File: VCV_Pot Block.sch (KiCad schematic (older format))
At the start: 18 parts, among them J14 Conn_01x08_Female, U3 CD74HC4067M

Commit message: Sub boards completed
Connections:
- net at U3.13 (S3): now also J14.3 (Pin_3); no longer J14.4 (Pin_4)
- net at U3.14 (S2): now also J14.4 (Pin_4); no longer J14.3 (Pin_3)
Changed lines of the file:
@@
 	1300 2400 2050 2400
 Wire Wire Line
-	1300 2600 2050 2600
-Wire Wire Line
 	1300 2500 2050 2500
-Wire Wire Line
-	1300 2700 2050 2700
 Wire Wire Line
 	1950 2800 1300 2800
@@
 Connection ~ 2550 1500
 NoConn ~ 1300 3100
+Wire Wire Line
+	1300 2600 1650 2600
+Wire Wire Line
+	1650 2600 1650 2700
+Wire Wire Line
+	1650 2700 2050 2700
+Wire Wire Line
+	2050 2600 1750 2600
+Wire Wire Line
+	1750 2600 1750 2650
+Wire Wire Line
+	1750 2650 1300 2650
+Wire Wire Line
+	1300 2650 1300 2700
 $EndSCHEMATC

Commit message: Tidy schematic / renumber components / complete daughter boards
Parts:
- J5: renamed from J14; value Conn_01x08_Female -> ~; symbol Connector:Conn_01x08_Female -> Connector:Conn_01x08_Male
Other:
- moved on the sheet: PT_1, PT_10, PT_11, PT_12, PT_13, PT_14, PT_15, PT_16, PT_2, PT_3, PT_4, PT_5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

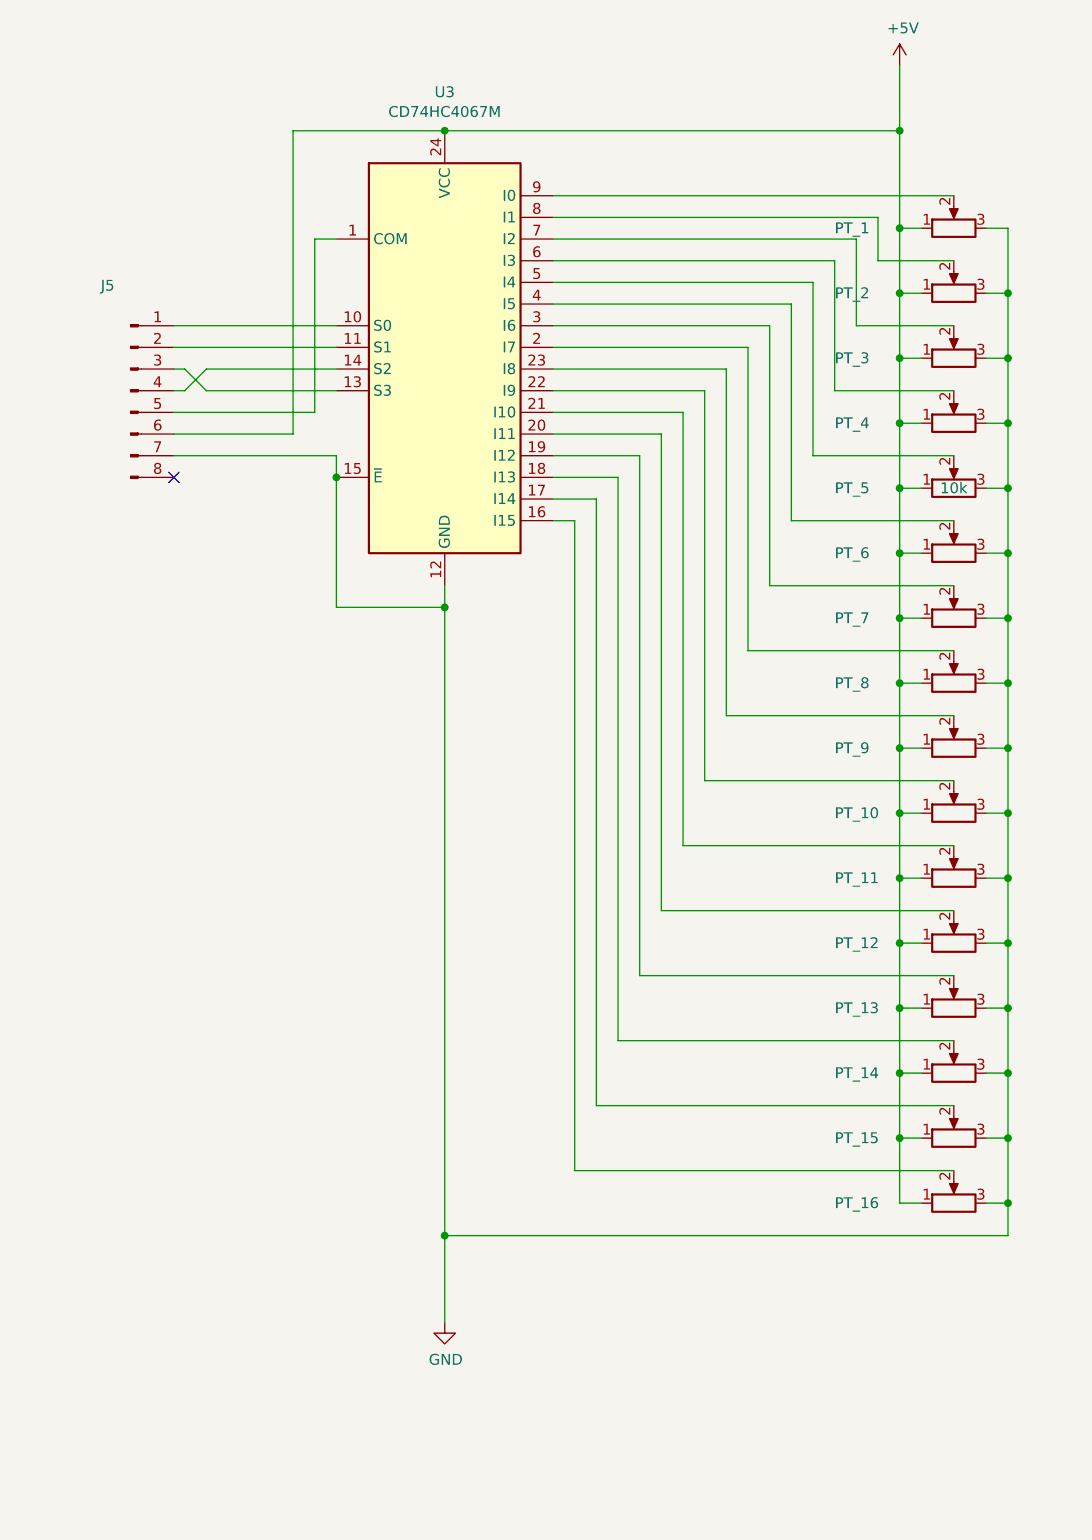
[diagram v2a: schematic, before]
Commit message: Redesign of upper boards
Added bussed resistors following Igor's correction to the schematic + tidied schematic.
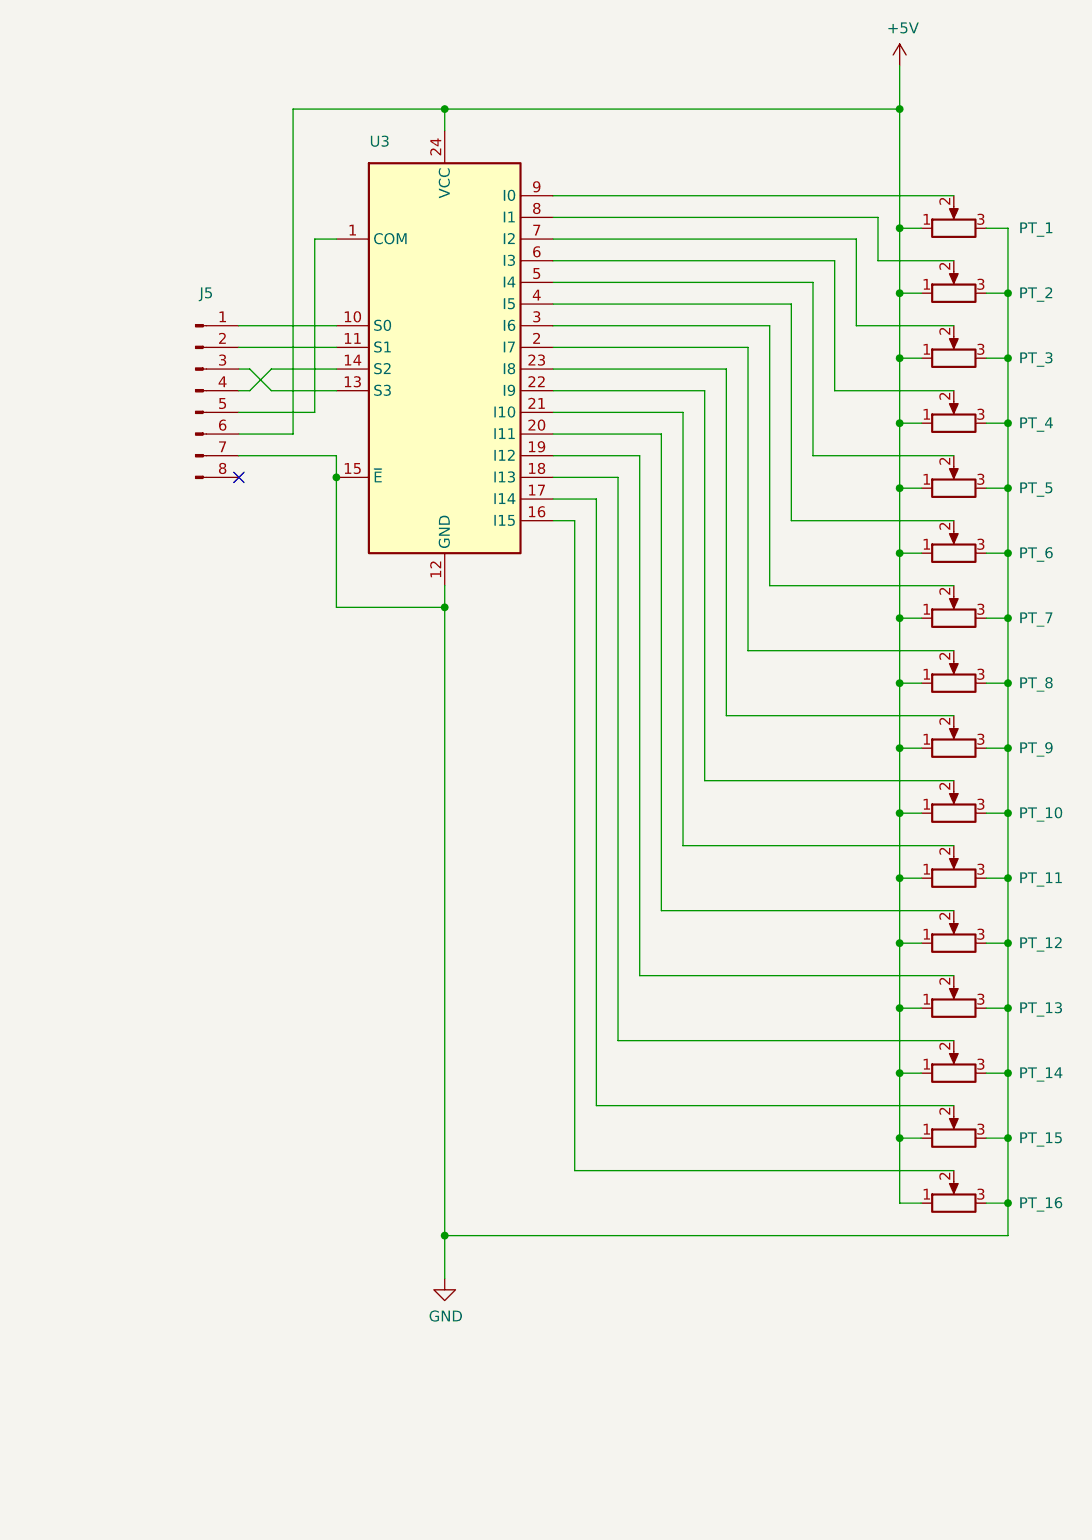
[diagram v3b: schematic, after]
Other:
- moved on the sheet: J5
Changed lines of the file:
@@
 U 1 1 5C26C20B
 P 5050 1700
-F 0 "PT_1" V 5050 2250 50  0000 R CNN
+F 0 "PT_1" V 5050 1400 50  0000 R CNN
 F 1 "10k" H 4980 1655 50  0001 R CNN
 F 2 "cunabulapress-footprints:Potentiometer_Alps_RK09K_Single_Vertical_Edit" H 5050 1700 50  0001 C CNN
@@
 U 1 1 5C26C26F
 P 5050 2000
-F 0 "PT_2" V 5050 2550 50  0000 R CNN
+F 0 "PT_2" V 5050 1700 50  0000 R CNN
 F 1 "10k" H 4980 1955 50  0001 R CNN
 F 2 "cunabulapress-footprints:Potentiometer_Alps_RK09K_Single_Vertical_Edit" H 5050 2000 50  0001 C CNN
@@
 U 1 1 5C26C8F7
 P 5050 2300
-F 0 "PT_3" V 5050 2850 50  0000 R CNN
+F 0 "PT_3" V 5050 2000 50  0000 R CNN
 F 1 "10k" H 4980 2255 50  0001 R CNN
 F 2 "cunabulapress-footprints:Potentiometer_Alps_RK09K_Single_Vertical_Edit" H 5050 2300 50  0001 C CNN
@@
 U 1 1 5C26CB54
 P 5050 2600
-F 0 "PT_4" V 5050 3150 50  0000 R CNN
+F 0 "PT_4" V 5050 2300 50  0000 R CNN
 F 1 "10k" H 4980 2555 50  0001 R CNN
 F 2 "cunabulapress-footprints:Potentiometer_Alps_RK09K_Single_Vertical_Edit" H 5050 2600 50  0001 C CNN
@@
 U 1 1 5C26CB7C
 P 5050 2900
-F 0 "PT_5" V 5050 3450 50  0000 R CNN
-F 1 "10k" V 5050 2900 50  0000 C CNN
+F 0 "PT_5" V 5050 2600 50  0000 R CNN
+F 1 "10k" V 5050 2900 50  0001 C CNN
 F 2 "cunabulapress-footprints:Potentiometer_Alps_RK09K_Single_Vertical_Edit" H 5050 2900 50  0001 C CNN
 F 3 "~" H 5050 2900 50  0001 C CNN
@@
 U 1 1 5C26CBA6
 P 5050 3200
-F 0 "PT_6" V 5050 3750 50  0000 R CNN
+F 0 "PT_6" V 5050 2900 50  0000 R CNN
 F 1 "10k" H 4980 3155 50  0001 R CNN
 F 2 "cunabulapress-footprints:Potentiometer_Alps_RK09K_Single_Vertical_Edit" H 5050 3200 50  0001 C CNN
@@
 U 1 1 5C26CBD2
 P 5050 3500
-F 0 "PT_7" V 5050 4050 50  0000 R CNN
+F 0 "PT_7" V 5050 3200 50  0000 R CNN
 F 1 "10k" H 4980 3455 50  0001 R CNN
 F 2 "cunabulapress-footprints:Potentiometer_Alps_RK09K_Single_Vertical_Edit" H 5050 3500 50  0001 C CNN
@@
 U 1 1 5C26CDC5
 P 5050 3800
-F 0 "PT_8" V 5050 4350 50  0000 R CNN
+F 0 "PT_8" V 5050 3500 50  0000 R CNN
 F 1 "10k" H 4980 3755 50  0001 R CNN
 F 2 "cunabulapress-footprints:Potentiometer_Alps_RK09K_Single_Vertical_Edit" H 5050 3800 50  0001 C CNN
@@
 U 1 1 5C26D143
 P 5050 4100
-F 0 "PT_9" V 5050 4650 50  0000 R CNN
+F 0 "PT_9" V 5050 3800 50  0000 R CNN
 F 1 "10k" H 4980 4055 50  0001 R CNN
 F 2 "cunabulapress-footprints:Potentiometer_Alps_RK09K_Single_Vertical_Edit" H 5050 4100 50  0001 C CNN
@@
 U 1 1 5C26D193
 P 5050 4400
-F 0 "PT_10" V 5050 4950 50  0000 R CNN
+F 0 "PT_10" V 5050 4100 50  0000 R CNN
 F 1 "10k" H 4980 4355 50  0001 R CNN
 F 2 "cunabulapress-footprints:Potentiometer_Alps_RK09K_Single_Vertical_Edit" H 5050 4400 50  0001 C CNN
@@
 U 1 1 5C26D1C9
 P 5050 4700
-F 0 "PT_11" V 5050 5250 50  0000 R CNN
+F 0 "PT_11" V 5050 4400 50  0000 R CNN
 F 1 "10k" H 4980 4655 50  0001 R CNN
 F 2 "cunabulapress-footprints:Potentiometer_Alps_RK09K_Single_Vertical_Edit" H 5050 4700 50  0001 C CNN
@@
 U 1 1 5C26D201
 P 5050 5000
-F 0 "PT_12" V 5050 5550 50  0000 R CNN
+F 0 "PT_12" V 5050 4700 50  0000 R CNN
 F 1 "10k" H 4980 4955 50  0001 R CNN
 F 2 "cunabulapress-footprints:Potentiometer_Alps_RK09K_Single_Vertical_Edit" H 5050 5000 50  0001 C CNN
@@
 U 1 1 5C26D23B
 P 5050 5300
-F 0 "PT_13" V 5050 5850 50  0000 R CNN
+F 0 "PT_13" V 5050 5000 50  0000 R CNN
 F 1 "10k" H 4980 5255 50  0001 R CNN
 F 2 "cunabulapress-footprints:Potentiometer_Alps_RK09K_Single_Vertical_Edit" H 5050 5300 50  0001 C CNN
@@
 U 1 1 5C26D27D
 P 5050 5600
-F 0 "PT_14" V 5050 6150 50  0000 R CNN
+F 0 "PT_14" V 5050 5300 50  0000 R CNN
 F 1 "10k" H 4980 5555 50  0001 R CNN
 F 2 "cunabulapress-footprints:Potentiometer_Alps_RK09K_Single_Vertical_Edit" H 5050 5600 50  0001 C CNN
@@
 U 1 1 5C26D38D
 P 5050 5900
-F 0 "PT_15" V 5050 6450 50  0000 R CNN
+F 0 "PT_15" V 5050 5600 50  0000 R CNN
 F 1 "10k" H 4980 5855 50  0001 R CNN
 F 2 "cunabulapress-footprints:Potentiometer_Alps_RK09K_Single_Vertical_Edit" H 5050 5900 50  0001 C CNN
@@
 U 1 1 5C26D3C9
 P 5050 6200
-F 0 "PT_16" V 5050 6750 50  0000 R CNN
+F 0 "PT_16" V 5050 5900 50  0000 R CNN
 F 1 "10k" H 4980 6155 50  0001 R CNN
 F 2 "cunabulapress-footprints:Potentiometer_Alps_RK09K_Single_Vertical_Edit" H 5050 6200 50  0001 C CNN
@@
 L power:GND #PWR012
 U 1 1 5CB2CF9B
-P 2700 6750
-F 0 "#PWR012" H 2700 6500 50  0001 C CNN
-F 1 "GND" H 2705 6577 50  0000 C CNN
-F 2 "" H 2700 6750 50  0001 C CNN
-F 3 "" H 2700 6750 50  0001 C CNN
-	1    2700 6750
+P 2700 6550
+F 0 "#PWR012" H 2700 6300 50  0001 C CNN
+F 1 "GND" H 2705 6377 50  0000 C CNN
+F 2 "" H 2700 6550 50  0001 C CNN
+F 3 "" H 2700 6550 50  0001 C CNN
+	1    2700 6550
 	1    0    0    -1
 $EndComp
@@
 Wire Wire Line
 	5300 4100 5300 4400
-Wire Wire Line
-	4800 950  4800 1250
 $Comp
 L 74xx:CD74HC4067M U3
 U 1 1 5C4B03F9
 P 2700 2250
-F 0 "U3" H 2700 3428 50  0000 C CNN
-F 1 "CD74HC4067M" H 2700 3337 50  0000 C CNN
+F 0 "U3" H 2400 3200 50  0000 C CNN
+F 1 "CD74HC4067M" H 2700 3337 50  0001 C CNN
 F 2 "Package_SO:SOIC-24W_7.5x15.4mm_P1.27mm" H 3600 1250 50  0001 C CIN
 F 3 "http://www.ti.com/lit/ds/symlink/cd74hc4067.pdf" H 2350 3100 50  0001 C CNN
@@
 	3300 6050 5050 6050
 Wire Wire Line
-	2700 1250 4800 1250
-Connection ~ 4800 1250
-Wire Wire Line
-	4800 1250 4800 1700
-Wire Wire Line
 	2700 3350 2700 3450
 Wire Wire Line
 	2700 6350 5300 6350
-Connection ~ 2700 6350
-Wire Wire Line
-	2700 6350 2700 6750
 Wire Wire Line
 	2200 1750 2100 1750
-Wire Wire Line
-	2200 2850 2200 3450
 Wire Wire Line
 	2200 3450 2700 3450
@@
 L Connector:Conn_01x08_Male J5
 U 1 1 5CCF4899
-P 1250 2450
-F 0 "J5" H 1144 2935 50  0000 C CNN
-F 1 "~" H 1144 2844 50  0000 C CNN
-F 2 "cunabulapress-footprints:Connector_TE_Connectivity_Micro-MaTch_8_Position_Female" H 1250 2450 50  0001 C CNN
-F 3 "~" H 1250 2450 50  0001 C CNN
-	1    1250 2450
+P 1550 2450
+F 0 "J5" H 1600 2900 50  0000 C CNN
+F 1 "~" H 1444 2844 50  0000 C CNN
+F 2 "cunabulapress-footprints:Connector_TE_Connectivity_Micro-MaTch_8_Position_Female" H 1550 2450 50  0001 C CNN
+F 3 "~" H 1550 2450 50  0001 C CNN
+	1    1550 2450
 	1    0    0    -1
 $EndComp
 Wire Wire Line
-	1450 2150 2200 2150
-Wire Wire Line
-	1450 2250 2200 2250
-Wire Wire Line
-	2100 2550 1450 2550
-Wire Wire Line
 	2100 1750 2100 2550
-Wire Wire Line
-	2000 1250 2000 2650
-Wire Wire Line
-	2000 2650 1450 2650
+NoConn ~ 1750 2850
+Wire Wire Line
+	1800 2350 1900 2450
+Wire Wire Line
+	1900 2350 1800 2450
+Wire Wire Line
+	1800 2350 1750 2350
+Wire Wire Line
+	1750 2450 1800 2450
+Wire Wire Line
+	1750 2150 2200 2150
+Wire Wire Line
+	1750 2250 2200 2250
+Wire Wire Line
+	1900 2350 2200 2350
+Wire Wire Line
+	1900 2450 2200 2450
+Wire Wire Line
+	2100 2550 1750 2550
+Wire Wire Line
+	1750 2650 2000 2650
+Wire Wire Line
+	1750 2750 2200 2750
+Connection ~ 2200 2850
 Wire Wire Line
 	2200 2750 2200 2850
-Connection ~ 2200 2850
-Wire Wire Line
-	1450 2750 2200 2750
-Wire Wire Line
-	2000 1250 2700 1250
-Connection ~ 2700 1250
-NoConn ~ 1450 2850
-Wire Wire Line
-	1500 2350 1600 2450
-Wire Wire Line
-	1600 2450 2200 2450
-Wire Wire Line
-	1600 2350 1500 2450
-Wire Wire Line
-	1600 2350 2200 2350
-Wire Wire Line
-	1500 2350 1450 2350
-Wire Wire Line
-	1450 2450 1500 2450
+Wire Wire Line
+	2200 2850 2200 3450
+Wire Wire Line
+	4800 950  4800 1150
+Wire Wire Line
+	2000 1150 2700 1150
+Wire Wire Line
+	2700 1150 2700 1250
+Wire Wire Line
+	2000 1150 2000 2650
+Wire Wire Line
+	2700 1150 4800 1150
+Connection ~ 2700 1150
+Connection ~ 4800 1150
+Wire Wire Line
+	4800 1150 4800 1700
+Wire Wire Line
+	2700 6350 2700 6550
+Connection ~ 2700 6350
 $EndSCHEMATC

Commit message: Further cleanup and placement
Removed all the connectors to the rails as they're irrelevant to the top boards.

Added all the support headers.

Need to work out the correct routing for the headers but the placement is correct.
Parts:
- added JX07, JX08, JX09: Conn_02x03_Odd_Even, Connector_PinHeader_2.54mm:PinHeader_2x03_P2.54mm_Vertical, symbol Connector_Generic:Conn_02x03_Odd_Even
- J5: footprint cunabulapress-footprints:Connector_TE_Connectivity_Micro-MaTch_8_Position_Female -> Connector_PinHeader_2.54mm:PinHeader_2x03_P2.54mm_Vertical; symbol Connector:Conn_01x08_Male -> Connector:Conn_01x06_Male
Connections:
- net GND: now also JX09.1 (Pin_1), JX09.2 (Pin_2), JX09.3 (Pin_3), JX09.4 (Pin_4), JX09.5 (Pin_5), JX09.6 (Pin_6); no longer J5.7 (Pin_7)
- no-connect marks 1 -> 12
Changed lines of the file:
@@
 $Descr A4 11693 8268
 encoding utf-8
-Sheet 4 9
+Sheet 4 8
 Title "cp_midi_controller_002"
 Date "2019-01-13"
-Rev "v1"
+Rev "v3"
 Comp "Cunabula Press"
 Comment1 ""
@@
 	1    5050 6200
 	0    -1   -1   0
-$EndComp
-$Comp
-L power:GND #PWR012
-U 1 1 5CB2CF9B
-P 2700 6550
-F 0 "#PWR012" H 2700 6300 50  0001 C CNN
-F 1 "GND" H 2705 6377 50  0000 C CNN
-F 2 "" H 2700 6550 50  0001 C CNN
-F 3 "" H 2700 6550 50  0001 C CNN
-	1    2700 6550
-	1    0    0    -1
 $EndComp
 Wire Wire Line
@@
 	2700 3450 2700 6350
 $Comp
-L Connector:Conn_01x08_Male J5
+L Connector:Conn_01x06_Male J5
 U 1 1 5CCF4899
-P 1550 2450
-F 0 "J5" H 1600 2900 50  0000 C CNN
-F 1 "~" H 1444 2844 50  0000 C CNN
-F 2 "cunabulapress-footprints:Connector_TE_Connectivity_Micro-MaTch_8_Position_Female" H 1550 2450 50  0001 C CNN
-F 3 "~" H 1550 2450 50  0001 C CNN
-	1    1550 2450
+P 1550 2350
+F 0 "J5" H 1600 2800 50  0000 C CNN
+F 1 "~" H 1444 2744 50  0000 C CNN
+F 2 "Connector_PinHeader_2.54mm:PinHeader_2x03_P2.54mm_Vertical" H 1550 2350 50  0001 C CNN
+F 3 "~" H 1550 2350 50  0001 C CNN
+	1    1550 2350
 	1    0    0    -1
 $EndComp
 Wire Wire Line
 	2100 1750 2100 2550
-NoConn ~ 1750 2850
 Wire Wire Line
 	1800 2350 1900 2450
@@
 Wire Wire Line
 	1750 2650 2000 2650
-Wire Wire Line
-	1750 2750 2200 2750
-Connection ~ 2200 2850
-Wire Wire Line
-	2200 2750 2200 2850
 Wire Wire Line
 	2200 2850 2200 3450
@@
 Wire Wire Line
 	4800 1150 4800 1700
-Wire Wire Line
-	2700 6350 2700 6550
+$Comp
+L power:GND #PWR?
+U 1 1 5D8F0D62
+P 2700 7450
+AR Path="/5C4B73B3/5D8F0D62" Ref="#PWR?"  Part="1"
+AR Path="/5C3B66BD/5D8F0D62" Ref="#PWR0101"  Part="1"
+F 0 "#PWR0101" H 2700 7200 50  0001 C CNN
+F 1 "GND" H 2705 7277 50  0000 C CNN
+F 2 "" H 2700 7450 50  0001 C CNN
+F 3 "" H 2700 7450 50  0001 C CNN
+	1    2700 7450
+	1    0    0    -1
+$EndComp
+$Comp
+L Connector_Generic:Conn_02x03_Odd_Even JX?
+U 1 1 5D8F0D68
+P 950 7000
+AR Path="/5C4B73B3/5D8F0D68" Ref="JX?"  Part="1"
+AR Path="/5C3B66BD/5D8F0D68" Ref="JX07"  Part="1"
+F 0 "JX07" H 1000 7225 50  0000 C CNN
+F 1 "Conn_02x03_Odd_Even" H 1000 7226 50  0001 C CNN
+F 2 "Connector_PinHeader_2.54mm:PinHeader_2x03_P2.54mm_Vertical" H 950 7000 50  0001 C CNN
+F 3 "~" H 950 7000 50  0001 C CNN
+	1    950  7000
+	1    0    0    -1
+$EndComp
+$Comp
+L Connector_Generic:Conn_02x03_Odd_Even JX?
+U 1 1 5D8F0D6F
+P 2150 7000
+AR Path="/5C4B73B3/5D8F0D6F" Ref="JX?"  Part="1"
+AR Path="/5C3B66BD/5D8F0D6F" Ref="JX09"  Part="1"
+F 0 "JX09" H 2200 7225 50  0000 C CNN
+F 1 "Conn_02x03_Odd_Even" H 2200 7226 50  0001 C CNN
+F 2 "Connector_PinHeader_2.54mm:PinHeader_2x03_P2.54mm_Vertical" H 2150 7000 50  0001 C CNN
+F 3 "~" H 2150 7000 50  0001 C CNN
+	1    2150 7000
+	1    0    0    -1
+$EndComp
+Wire Wire Line
+	2700 7250 2700 7450
+Wire Wire Line
+	2450 6900 2450 7000
+Wire Wire Line
+	2450 7250 2700 7250
+Connection ~ 2450 7000
+Wire Wire Line
+	2450 7000 2450 7100
+Connection ~ 2450 7100
+Wire Wire Line
+	2450 7100 2450 7250
+$Comp
+L Connector_Generic:Conn_02x03_Odd_Even JX?
+U 1 1 5D8F0D7F
+P 1550 7000
+AR Path="/5C4B73B3/5D8F0D7F" Ref="JX?"  Part="1"
+AR Path="/5C3B66BD/5D8F0D7F" Ref="JX08"  Part="1"
+F 0 "JX08" H 1600 7225 50  0000 C CNN
+F 1 "Conn_02x03_Odd_Even" H 1600 7226 50  0001 C CNN
+F 2 "Connector_PinHeader_2.54mm:PinHeader_2x03_P2.54mm_Vertical" H 1550 7000 50  0001 C CNN
+F 3 "~" H 1550 7000 50  0001 C CNN
+	1    1550 7000
+	1    0    0    -1
+$EndComp
+Wire Wire Line
+	1900 6900 1900 7000
+Wire Wire Line
+	1900 7250 2450 7250
+Connection ~ 2450 7250
+Wire Wire Line
+	1950 7100 1900 7100
+Connection ~ 1900 7100
+Wire Wire Line
+	1900 7100 1900 7250
+Wire Wire Line
+	1950 7000 1900 7000
+Connection ~ 1900 7000
+Wire Wire Line
+	1900 7000 1900 7100
+Wire Wire Line
+	1950 6900 1900 6900
+NoConn ~ 1850 6900
+NoConn ~ 1850 7000
+NoConn ~ 1850 7100
+NoConn ~ 1350 7100
+NoConn ~ 1350 7000
+NoConn ~ 1350 6900
+NoConn ~ 1250 6900
+NoConn ~ 1250 7000
+NoConn ~ 1250 7100
+NoConn ~ 750  6900
+NoConn ~ 750  7000
+NoConn ~ 750  7100
+Wire Wire Line
+	2700 6350 2700 7250
 Connection ~ 2700 6350
+Connection ~ 2700 7250
 $EndSCHEMATC

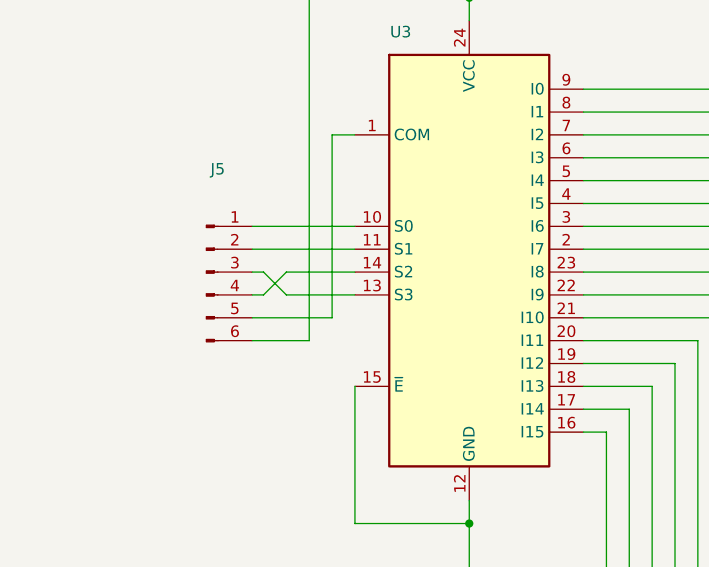
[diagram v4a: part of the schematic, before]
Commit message: Fixed S0-S3 Rail, added LEDS
Was an error on the schematic, easily fixed without changing the traces, glad I left it before deleting them all.

LEDs and relate resistors are in.
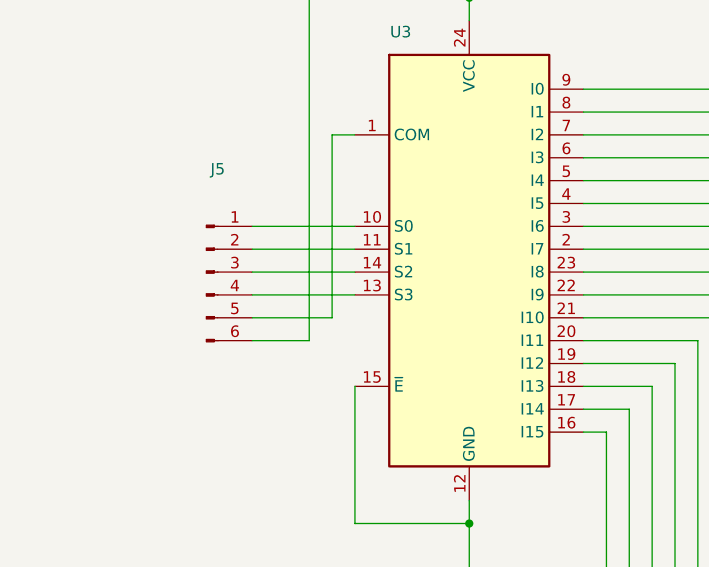
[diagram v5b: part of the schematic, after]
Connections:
- net at U3.13 (S3): now also J5.4 (Pin_4); no longer J5.3 (Pin_3)
- net at U3.14 (S2): now also J5.3 (Pin_3); no longer J5.4 (Pin_4)
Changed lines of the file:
@@
 	2100 1750 2100 2550
-Wire Wire Line
-	1800 2350 1900 2450
-Wire Wire Line
-	1900 2350 1800 2450
-Wire Wire Line
-	1800 2350 1750 2350
-Wire Wire Line
-	1750 2450 1800 2450
 Wire Wire Line
 	1750 2150 2200 2150
 Wire Wire Line
 	1750 2250 2200 2250
-Wire Wire Line
-	1900 2350 2200 2350
-Wire Wire Line
-	1900 2450 2200 2450
 Wire Wire Line
 	2100 2550 1750 2550
@@
 Connection ~ 2700 6350
 Connection ~ 2700 7250
+Wire Wire Line
+	1750 2350 2200 2350
+Wire Wire Line
+	1750 2450 2200 2450
 $EndSCHEMATC
